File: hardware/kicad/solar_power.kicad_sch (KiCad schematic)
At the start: 12 parts, among them U3 AEM10941-QFN

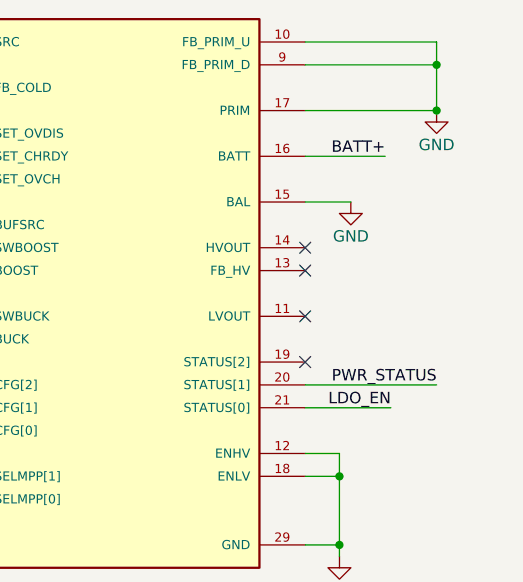
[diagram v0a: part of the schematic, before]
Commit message: fix label
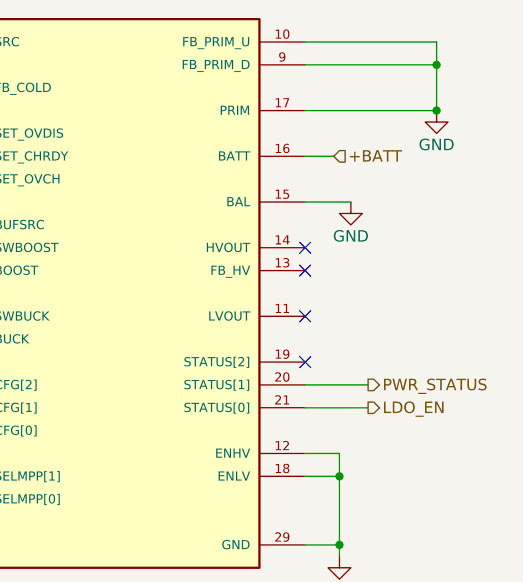
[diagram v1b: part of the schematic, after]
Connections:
- net BATT+ renamed +BATT
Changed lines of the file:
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@@
+    (stroke (width 0) (type default))
+  )
+  (wire (pts (xy 215.9 95.885) (xy 222.885 95.885))
     (stroke (width 0) (type default))
   )
@@
     (stroke (width 0) (type default))
   )
-  (wire (pts (xy 215.9 98.425) (xy 225.425 98.425))
-    (stroke (width 0) (type default))
-  )
   (wire (pts (xy 103.505 72.39) (xy 103.505 74.93))
     (stroke (width 0) (type default))
@@
     (stroke (width 0) (type default))
   )
-  (wire (pts (xy 215.9 70.485) (xy 224.79 70.485))
-    (stroke (width 0) (type default))
-  )
   (wire (pts (xy 86.36 58.42) (xy 103.505 58.42))
     (stroke (width 0) (type default))
@@
   )
   (wire (pts (xy 175.26 75.565) (xy 142.24 75.565))
-    (stroke (width 0) (type default))
-  )
-  (wire (pts (xy 215.9 95.885) (xy 230.505 95.885))
     (stroke (width 0) (type default))
   )
@@
   )
   (wire (pts (xy 48.895 58.42) (xy 48.895 64.77))
+    (stroke (width 0) (type default))
+  )
+  (wire (pts (xy 215.9 70.485) (xy 219.075 70.485))
+    (stroke (width 0) (type default))
+  )
+  (wire (pts (xy 215.9 98.425) (xy 222.885 98.425))
     (stroke (width 0) (type default))
   )
@@
     (effects (font (size 1.27 1.27)) (justify left bottom))
   )
-  (label "BATT+" (at 224.79 70.485 180) (fields_autoplaced)
-    (effects (font (size 1.27 1.27)) (justify right bottom))
-  )
   (label "SOLAR+" (at 161.29 57.785 0) (fields_autoplaced)
     (effects (font (size 1.27 1.27)) (justify left bottom))
@@
     (effects (font (size 1.27 1.27)) (justify left bottom))
   )
-  (label "PWR_STATUS" (at 230.505 95.885 180) (fields_autoplaced)
-    (effects (font (size 1.27 1.27)) (justify right bottom))
-  )
   (label "BUCK" (at 170.18 90.805 0) (fields_autoplaced)
     (effects (font (size 1.27 1.27)) (justify left bottom))
@@
     (effects (font (size 1.27 1.27)) (justify left bottom))
   )
-  (label "LDO_EN" (at 225.425 98.425 180) (fields_autoplaced)
-    (effects (font (size 1.27 1.27)) (justify right bottom))
-  )
   (label "SOLAR+" (at 48.895 58.42 0) (fields_autoplaced)
     (effects (font (size 1.27 1.27)) (justify left bottom))
   )
+  (hierarchical_label "LDO_EN" (shape output) (at 222.885 98.425 0) (fields_autoplaced)
+    (effects (font (size 1.27 1.27)) (justify left))
+  )
+  (hierarchical_label "+BATT" (shape input) (at 219.075 70.485 0) (fields_autoplaced)
+    (effects (font (size 1.27 1.27)) (justify left))
+  )
+  (hierarchical_label "PWR_STATUS" (shape output) (at 222.885 95.885 0) (fields_autoplaced)
+    (effects (font (size 1.27 1.27)) (justify left))
+  )
   (symbol (lib_id "power:GND") (at 162.56 98.425 0) (unit 1)

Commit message: schematic restructure update
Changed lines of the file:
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@@
+    (stroke (width 0) (type default))
+  )
+  (wire (pts (xy 223.52 70.485) (xy 223.52 69.215))
     (stroke (width 0) (type default))
   )
@@
     (stroke (width 0) (type default))
   )
-  (wire (pts (xy 215.9 70.485) (xy 219.075 70.485))
+  (wire (pts (xy 215.9 70.485) (xy 223.52 70.485))
     (stroke (width 0) (type default))
   )
@@
     (stroke (width 0) (type default))
   )
+  (wire (pts (xy 210.82 45.72) (xy 212.725 45.72))
+    (stroke (width 0) (type default))
+  )
   (wire (pts (xy 162.56 95.885) (xy 162.56 98.425))
     (stroke (width 0) (type default))
@@
   )
   (wire (pts (xy 163.195 106.045) (xy 163.195 108.585))
+    (stroke (width 0) (type default))
+  )
+  (wire (pts (xy 210.82 43.18) (xy 210.82 45.72))
     (stroke (width 0) (type default))
   )
@@
     (effects (font (size 1.27 1.27)) (justify left))
   )
-  (hierarchical_label "+BATT" (shape input) (at 219.075 70.485 0) (fields_autoplaced)
+  (hierarchical_label "+BATT" (shape bidirectional) (at 212.725 45.72 0) (fields_autoplaced)
     (effects (font (size 1.27 1.27)) (justify left))
   )
@@
         )
         (path "/59b4123e-c7be-466b-a5db-658b8f0c1171/8a163738-8cdd-43d1-ab87-ebdfd2811ec1"
-          (reference "#PWR024") (unit 1)
+          (reference "#PWR047") (unit 1)
         )
       )
@@
         )
         (path "/59b4123e-c7be-466b-a5db-658b8f0c1171/8a163738-8cdd-43d1-ab87-ebdfd2811ec1"
-          (reference "C7") (unit 1)
+          (reference "C23") (unit 1)
         )
       )
@@
         )
         (path "/59b4123e-c7be-466b-a5db-658b8f0c1171/8a163738-8cdd-43d1-ab87-ebdfd2811ec1"
-          (reference "L2") (unit 1)
+          (reference "L4") (unit 1)
         )
       )
@@
         )
         (path "/59b4123e-c7be-466b-a5db-658b8f0c1171/8a163738-8cdd-43d1-ab87-ebdfd2811ec1"
-          (reference "#PWR027") (unit 1)
+          (reference "#PWR049") (unit 1)
         )
       )
@@
         )
         (path "/59b4123e-c7be-466b-a5db-658b8f0c1171/8a163738-8cdd-43d1-ab87-ebdfd2811ec1"
-          (reference "#PWR025") (unit 1)
+          (reference "#PWR048") (unit 1)
         )
       )
@@
         )
         (path "/59b4123e-c7be-466b-a5db-658b8f0c1171/8a163738-8cdd-43d1-ab87-ebdfd2811ec1"
-          (reference "#PWR030") (unit 1)
+          (reference "#PWR052") (unit 1)
         )
       )
@@
     )
   )
+  (symbol (lib_id "power:+BATT") (at 223.52 69.215 0) (unit 1)
+    (in_bom yes) (on_board yes) (dnp no)
+    (property "Reference" "#PWR070" (at 223.52 73.025 0)
+      (effects (font (size 1.27 1.27)) hide)
+    )
+    (property "Value" "+BATT" (at 219.075 67.945 0)
+      (effects (font (size 1.27 1.27)))
+    )
+    (property "Footprint" "" (at 223.52 69.215 0)
+      (effects (font (size 1.27 1.27)) hide)
+    )
+    (property "Datasheet" "" (at 223.52 69.215 0)
+      (effects (font (size 1.27 1.27)) hide)
+    )
+    (pin "1")
+    (instances
+      (project "plantpal"
+        (path "/59b4123e-c7be-466b-a5db-658b8f0c1171"
+          (reference "#PWR070") (unit 1)
+        )
+        (path "/59b4123e-c7be-466b-a5db-658b8f0c1171/7fda2409-1758-4461-822b-801ba75fe202"
+          (reference "#PWR050") (unit 1)
+        )
+        (path "/59b4123e-c7be-466b-a5db-658b8f0c1171/8a163738-8cdd-43d1-ab87-ebdfd2811ec1"
+          (reference "#PWR051") (unit 1)
+        )
+      )
+      (project "bwlr1e-prog"
+        (path "/630c8da6-5464-4eef-824d-89618087f4b4"
+          (reference "#PWR018") (unit 1)
+        )
+      )
+      (project "feather_rak3172"
+        (path "/a1545928-1195-40b9-b3c4-78f837012afb"
+          (reference "#PWR0131") (unit 1)
+        )
+      )
+    )
+  )
   (symbol (lib_name "Solar_Cell_1") (lib_id "Device:Solar_Cell") (at 48.895 69.85 0) (unit 1)
     (in_bom yes) (on_board yes) (dnp no)
@@
         )
         (path "/59b4123e-c7be-466b-a5db-658b8f0c1171/8a163738-8cdd-43d1-ab87-ebdfd2811ec1"
-          (reference "#PWR020") (unit 1)
+          (reference "#PWR045") (unit 1)
         )
       )
@@
         )
         (path "/59b4123e-c7be-466b-a5db-658b8f0c1171/8a163738-8cdd-43d1-ab87-ebdfd2811ec1"
-          (reference "C5") (unit 1)
+          (reference "C21") (unit 1)
         )
       )
@@
         )
         (path "/59b4123e-c7be-466b-a5db-658b8f0c1171/8a163738-8cdd-43d1-ab87-ebdfd2811ec1"
-          (reference "TP2") (unit 1)
+          (reference "TP3") (unit 1)
         )
       )
@@
         )
         (path "/59b4123e-c7be-466b-a5db-658b8f0c1171/8a163738-8cdd-43d1-ab87-ebdfd2811ec1"
-          (reference "C6") (unit 1)
+          (reference "C22") (unit 1)
         )
       )
@@
         )
         (path "/59b4123e-c7be-466b-a5db-658b8f0c1171/8a163738-8cdd-43d1-ab87-ebdfd2811ec1"
-          (reference "#PWR021") (unit 1)
+          (reference "#PWR046") (unit 1)
         )
       )
@@
         )
         (path "/59b4123e-c7be-466b-a5db-658b8f0c1171/8a163738-8cdd-43d1-ab87-ebdfd2811ec1"
-          (reference "TP3") (unit 1)
+          (reference "TP4") (unit 1)
         )
       )
@@
         )
         (path "/59b4123e-c7be-466b-a5db-658b8f0c1171/8a163738-8cdd-43d1-ab87-ebdfd2811ec1"
-          (reference "#PWR05") (unit 1)
+          (reference "#PWR044") (unit 1)
         )
       )
@@
         )
         (path "/59b4123e-c7be-466b-a5db-658b8f0c1171/8a163738-8cdd-43d1-ab87-ebdfd2811ec1"
-          (reference "#PWR029") (unit 1)
+          (reference "#PWR050") (unit 1)
         )
       )
@@
         (path "/630c8da6-5464-4eef-824d-89618087f4b4"
           (reference "#PWR0118") (unit 1)
+        )
+      )
+    )
+  )
+  (symbol (lib_id "power:+BATT") (at 210.82 43.18 0) (unit 1)
+    (in_bom yes) (on_board yes) (dnp no)
+    (property "Reference" "#PWR070" (at 210.82 46.99 0)
+      (effects (font (size 1.27 1.27)) hide)
+    )
+    (property "Value" "+BATT" (at 206.375 41.91 0)
+      (effects (font (size 1.27 1.27)))
+    )
+    (property "Footprint" "" (at 210.82 43.18 0)
+      (effects (font (size 1.27 1.27)) hide)
+    )
+    (property "Datasheet" "" (at 210.82 43.18 0)
+      (effects (font (size 1.27 1.27)) hide)
+    )
+    (pin "1")
+    (instances
+      (project "plantpal"
+        (path "/59b4123e-c7be-466b-a5db-658b8f0c1171"
+          (reference "#PWR070") (unit 1)
+        )
+        (path "/59b4123e-c7be-466b-a5db-658b8f0c1171/7fda2409-1758-4461-822b-801ba75fe202"
+          (reference "#PWR050") (unit 1)
+        )
+        (path "/59b4123e-c7be-466b-a5db-658b8f0c1171/8a163738-8cdd-43d1-ab87-ebdfd2811ec1"
+          (reference "#PWR083") (unit 1)
+        )
+      )
+      (project "bwlr1e-prog"
+        (path "/630c8da6-5464-4eef-824d-89618087f4b4"
+          (reference "#PWR018") (unit 1)
+        )
+      )
+      (project "feather_rak3172"
+        (path "/a1545928-1195-40b9-b3c4-78f837012afb"
+          (reference "#PWR0131") (unit 1)
         )
       )
@@
         )
         (path "/59b4123e-c7be-466b-a5db-658b8f0c1171/8a163738-8cdd-43d1-ab87-ebdfd2811ec1"
-          (reference "U3") (unit 1)
+          (reference "U4") (unit 1)
         )
       )
@@
         )
         (path "/59b4123e-c7be-466b-a5db-658b8f0c1171/8a163738-8cdd-43d1-ab87-ebdfd2811ec1"
-          (reference "L1") (unit 1)
-        )
-      )
+          (reference "L3") (unit 1)
+        )
+      )

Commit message: beautify schematic
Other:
- note added: "Sheets Connection"
- moved on the sheet: C14, C15, C17, L2, L3, SC1, SC2, SC3, SC4, TP4, TP5, U3

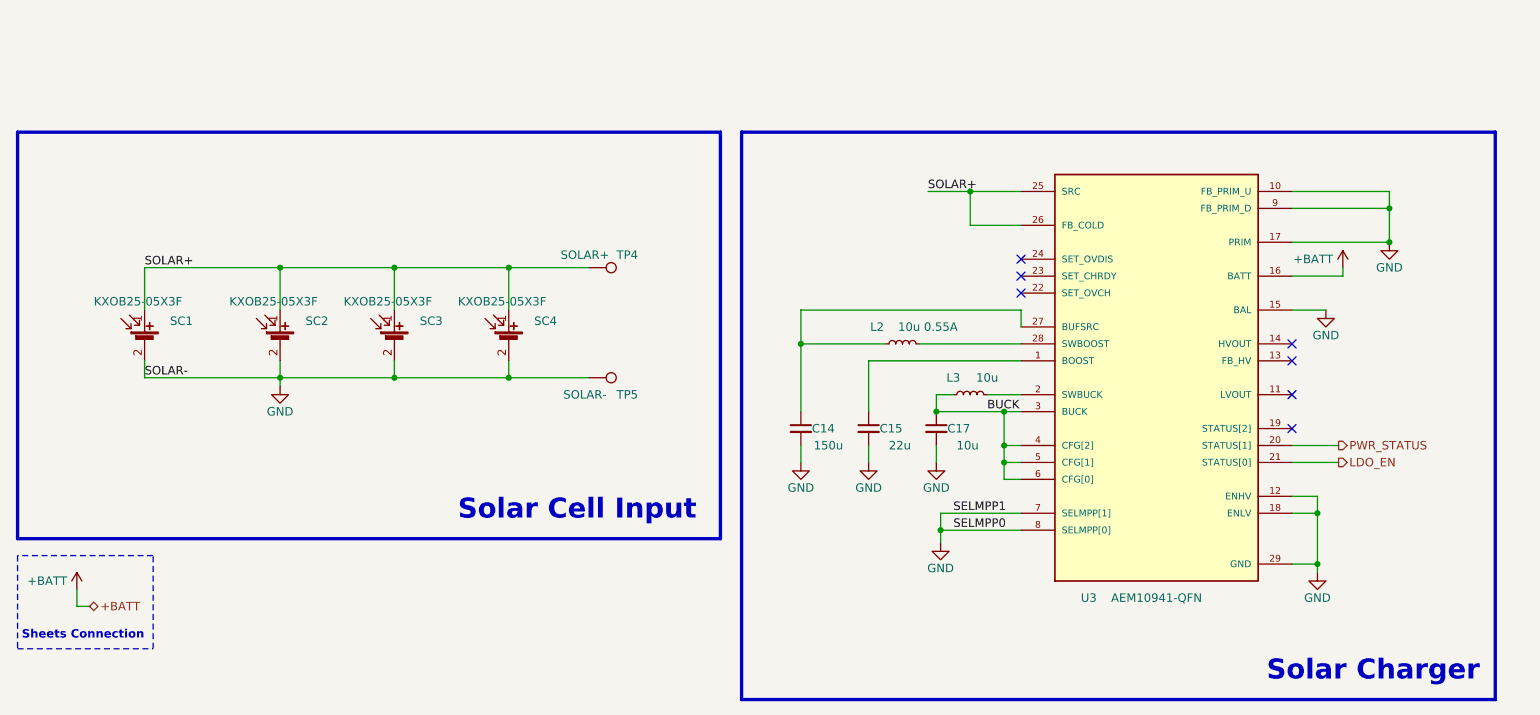
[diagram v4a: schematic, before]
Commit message: solar power schematic done
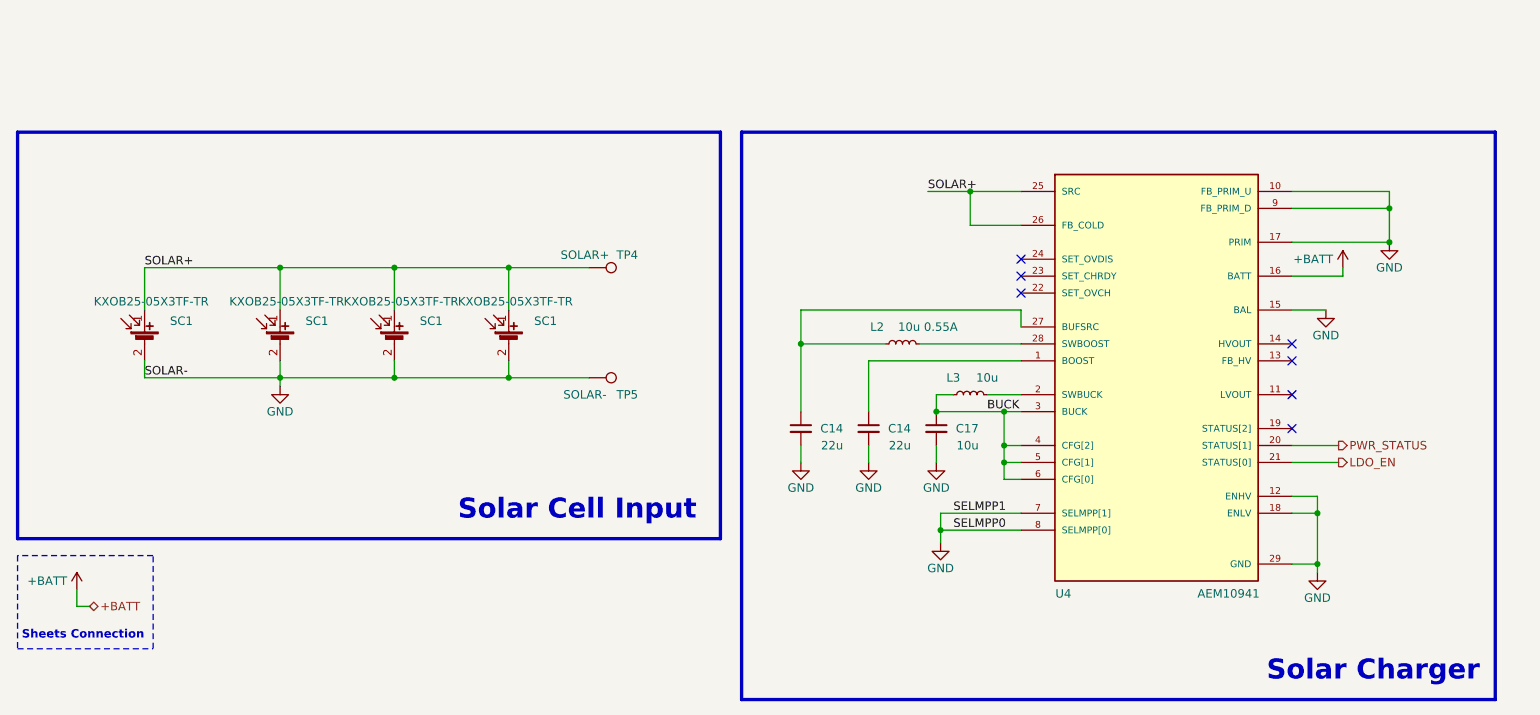
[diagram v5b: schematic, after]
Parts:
- removed C15: 22u, Capacitor_SMD:C_0603_1608Metric_Pad1.08x0.95mm_HandSolder, symbol Device:C_Small
- removed SC2, SC3, SC4: KXOB25-05X3F, Teapot:KXOB25-05X3F, symbol Device:Solar_Cell
- removed U3: AEM10941-QFN, Package_DFN_QFN:QFN-28-1EP_5x5mm_P0.5mm_EP3.35x3.35mm, symbol Teapot:AEM10941-QFN
- added C14: 22u, Capacitor_SMD:C_0603_1608Metric, symbol Device:C_Small
- added SC1 (x3): KXOB25-05X3TF-TR, plantpal:KXOB25-05X3F, symbol Device:Solar_Cell
- added U4: AEM10941, Package_DFN_QFN:QFN-28-1EP_5x5mm_P0.5mm_EP3.35x3.35mm, symbol plantpal:AEM10941-QFN
- C14: value 150u -> 22u; footprint Capacitor_SMD:C_1210_3225Metric -> Capacitor_SMD:C_0603_1608Metric; Distributor (none) -> LCSC; Distributor Link (none) -> https://www.lcsc.com/product-detail/Multilayer-Ceramic-Capa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; Distributor Part Number (none) -> C84419; Manufacturer (none) -> Murata Electronics; Manufacturer Part Number (none) -> GRM188R61A226ME15D; Mouser https://www.mouser.com/ProductDetail/Murata-Electronics/GRM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 -> (none); Part Description (none) -> Ceramic Capacitors 10V 22uF X5R ±20%
- C17: footprint Capacitor_SMD:C_0603_1608Metric_Pad1.08x0.95mm_HandSolder -> Capacitor_SMD:C_0603_1608Metric; Distributor (none) -> LCSC; Distributor Link (none) -> https://www.lcsc.com/product-detail/Multilayer-Ceramic-Capa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; Distributor Part Number (none) -> C19702; Manufacturer (none) -> Samsung Electro-Mechanics; Manufacturer Part Number (none) -> CL10A106KP8NNNC; Mouser https://www.mouser.com/ProductDetail/Murata-Electronics/GRM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 -> (none); Part Description (none) -> Ceramic Capacitor 10V 10uF X5R ±10%
- L2: footprint Teapot:IND_LPS4012-103MRB -> plantpal:IND_LPS4012-103MRB; Distributor (none) -> Mouser; Distributor Link (none) -> https://www.mouser.com/ProductDetail/Coilcraft/LPS4012-103M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; Distributor Part Number (none) -> 994-LPS4012-103MRC; Manufacturer (none) -> Coilcraft; Manufacturer Part Number (none) -> LPS4012-103MRC; Mouser https://www.mouser.com/ProductDetail/Coilcraft/LPS4012-103M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 -> (none); Part Description (none) -> Power Inductors - SMD 10uH Shld 20% 1.1A 350 mOhms
- L3: footprint Inductor_SMD:L_0603_1608Metric_Pad1.05x0.95mm_HandSolder -> Inductor_SMD:L_0603_1608Metric; Distributor (none) -> LCSC; Distributor Link (none) -> https://www.lcsc.com/product-detail/Inductors-SMD_TDK-MLZ16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; Distributor Part Number (none) -> C76798; Manufacturer (none) -> TDK; Manufacturer Part Number (none) -> MLZ1608M100WT000; Mouser https://www.mouser.com/ProductDetail/TDK/MLZ1608M100WT000?q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 -> (none); Part Description (none) -> Power Inductors 10uH ±20% 90mA 1.05Ω
- SC1: value KXOB25-05X3F -> KXOB25-05X3TF-TR; footprint Teapot:KXOB25-05X3F -> plantpal:KXOB25-05X3F; Distributor (none) -> Digikey; Distributor Link (none) -> https://www.digikey.com/en/products/detail/anysolar-ltd/KXO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; Distributor Part Number (none) -> 2994-KXOB25-05X3TF-TRCT-ND; Manufacturer (none) -> ANYSOLAR Ltd; Manufacturer Part Number (none) -> KXOB25-05X3TF-TR; Part Description (none) -> Solar Cell G3 Thin 2.07V 30.9MW
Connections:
- net +BATT: now also U4.16 (BATT)
- net BUCK: now also U4.3 (BUCK), U4.4 (CFG[2]), U4.5 (CFG[1]), U4.6 (CFG[0])
- net GND: now also C14.2, SC1.2 (-), SC1.2 (-), SC1.2 (-), U4.10 (FB_PRIM_U), U4.12 (ENHV), U4.15 (BAL), U4.17 (PRIM), U4.18 (ENLV), U4.29 (GND), U4.7 (SELMPP[1]), U4.8 (SELMPP[0]), U4.9 (FB_PRIM_D)
- net LDO_EN: now also U4.21 (STATUS[0])
- net PWR_STATUS: now also U4.20 (STATUS[1])
- net SOLAR+: now also SC1.1 (+), SC1.1 (+), SC1.1 (+), U4.25 (SRC), U4.26 (FB_COLD)
- net at L3.2: now also U4.2 (SWBUCK)
- net at C14.1, L2.1: now also U4.27 (BUFSRC)
- net at L2.2: now also U4.28 (SWBOOST)
- new net: C14.1, U4.1 (BOOST)

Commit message: clean-up
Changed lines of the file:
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@@
         )
         (path "/59b4123e-c7be-466b-a5db-658b8f0c1171/8a163738-8cdd-43d1-ab87-ebdfd2811ec1"
-          (reference "#PWR051") (unit 1)
+          (reference "#PWR054") (unit 1)
         )
       )
@@
         )
         (path "/59b4123e-c7be-466b-a5db-658b8f0c1171/8a163738-8cdd-43d1-ab87-ebdfd2811ec1"
-          (reference "C23") (unit 1)
+          (reference "C24") (unit 1)
         )
       )
@@
         )
         (path "/59b4123e-c7be-466b-a5db-658b8f0c1171/8a163738-8cdd-43d1-ab87-ebdfd2811ec1"
-          (reference "#PWR053") (unit 1)
+          (reference "#PWR056") (unit 1)
         )
       )
@@
         )
         (path "/59b4123e-c7be-466b-a5db-658b8f0c1171/8a163738-8cdd-43d1-ab87-ebdfd2811ec1"
-          (reference "C22") (unit 1)
+          (reference "C23") (unit 1)
         )
       )
@@
         )
         (path "/59b4123e-c7be-466b-a5db-658b8f0c1171/8a163738-8cdd-43d1-ab87-ebdfd2811ec1"
-          (reference "#PWR052") (unit 1)
+          (reference "#PWR055") (unit 1)
         )
       )
@@
         )
         (path "/59b4123e-c7be-466b-a5db-658b8f0c1171/8a163738-8cdd-43d1-ab87-ebdfd2811ec1"
-          (reference "#PWR056") (unit 1)
+          (reference "#PWR059") (unit 1)
         )
       )
@@
         )
         (path "/59b4123e-c7be-466b-a5db-658b8f0c1171/8a163738-8cdd-43d1-ab87-ebdfd2811ec1"
-          (reference "#PWR055") (unit 1)
+          (reference "#PWR058") (unit 1)
         )
       )
@@
         )
         (path "/59b4123e-c7be-466b-a5db-658b8f0c1171/8a163738-8cdd-43d1-ab87-ebdfd2811ec1"
-          (reference "#PWR049") (unit 1)
+          (reference "#PWR052") (unit 1)
         )
       )
@@
         )
         (path "/59b4123e-c7be-466b-a5db-658b8f0c1171/8a163738-8cdd-43d1-ab87-ebdfd2811ec1"
-          (reference "C21") (unit 1)
+          (reference "C22") (unit 1)
         )
       )
@@
         )
         (path "/59b4123e-c7be-466b-a5db-658b8f0c1171/8a163738-8cdd-43d1-ab87-ebdfd2811ec1"
-          (reference "#PWR050") (unit 1)
+          (reference "#PWR053") (unit 1)
         )
       )
@@
         )
         (path "/59b4123e-c7be-466b-a5db-658b8f0c1171/8a163738-8cdd-43d1-ab87-ebdfd2811ec1"
-          (reference "#PWR048") (unit 1)
+          (reference "#PWR051") (unit 1)
         )
       )
@@
         )
         (path "/59b4123e-c7be-466b-a5db-658b8f0c1171/8a163738-8cdd-43d1-ab87-ebdfd2811ec1"
-          (reference "#PWR054") (unit 1)
+          (reference "#PWR057") (unit 1)
         )
       )
@@
         )
         (path "/59b4123e-c7be-466b-a5db-658b8f0c1171/8a163738-8cdd-43d1-ab87-ebdfd2811ec1"
-          (reference "#PWR047") (unit 1)
+          (reference "#PWR050") (unit 1)
         )
       )
@@
       (effects (font (size 1.27 1.27)) (justify left))
     )
-    (property "Value" "KXOB25-05X3TF-TR" (at 73.66 83.82 0)
+    (property "Value" "KXOB25-05X3TF-TR" (at 71.12 92.71 0)
       (effects (font (size 1.27 1.27)) (justify left))
     )
@@
       (effects (font (size 1.27 1.27)) (justify left))
     )
-    (property "Value" "KXOB25-05X3TF-TR" (at 107.95 83.82 0)
+    (property "Value" "KXOB25-05X3TF-TR" (at 105.41 93.345 0)
       (effects (font (size 1.27 1.27)) (justify left))
     )
